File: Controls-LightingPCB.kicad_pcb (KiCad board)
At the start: 2 copper layers, 63.5 x 114.3 mm, 65 parts, among them J1 MinionConn, J2 Backup, SW1 HAZARD, SW2 CRUISE_SET, SW3 CRUISE, SW4 F/R_SW, SW5 HEADLIGHT_SW, SW6 BACKUP_SW, SW7 TURN_SIGNAL_SW, SW8 REGEN_SW, U1 LTC6820, U2 HX1188FNL, U3 MCP23S17_SO, U4 RI3-1205S, U5 NCP1117-3.3_SOT223

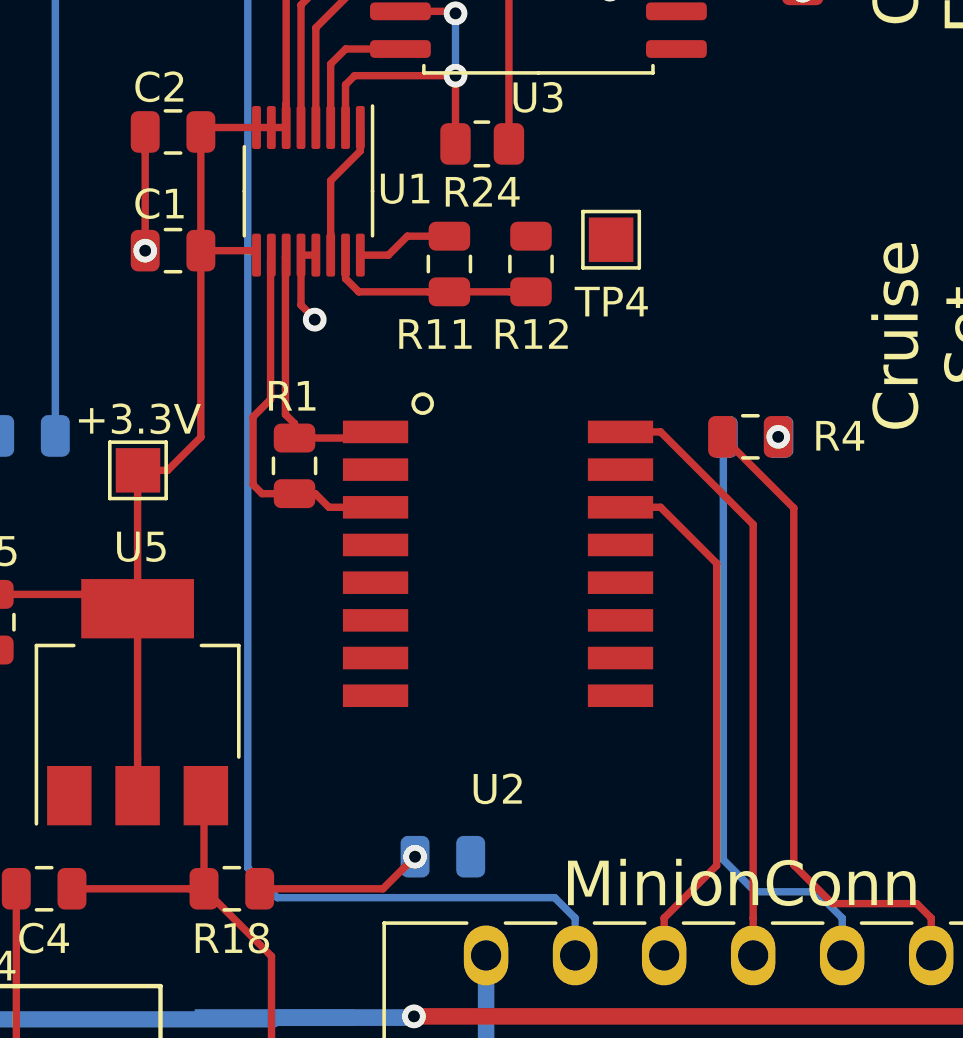
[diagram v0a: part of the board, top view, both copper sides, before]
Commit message: Remove some ground plane underneath isoSPI signals
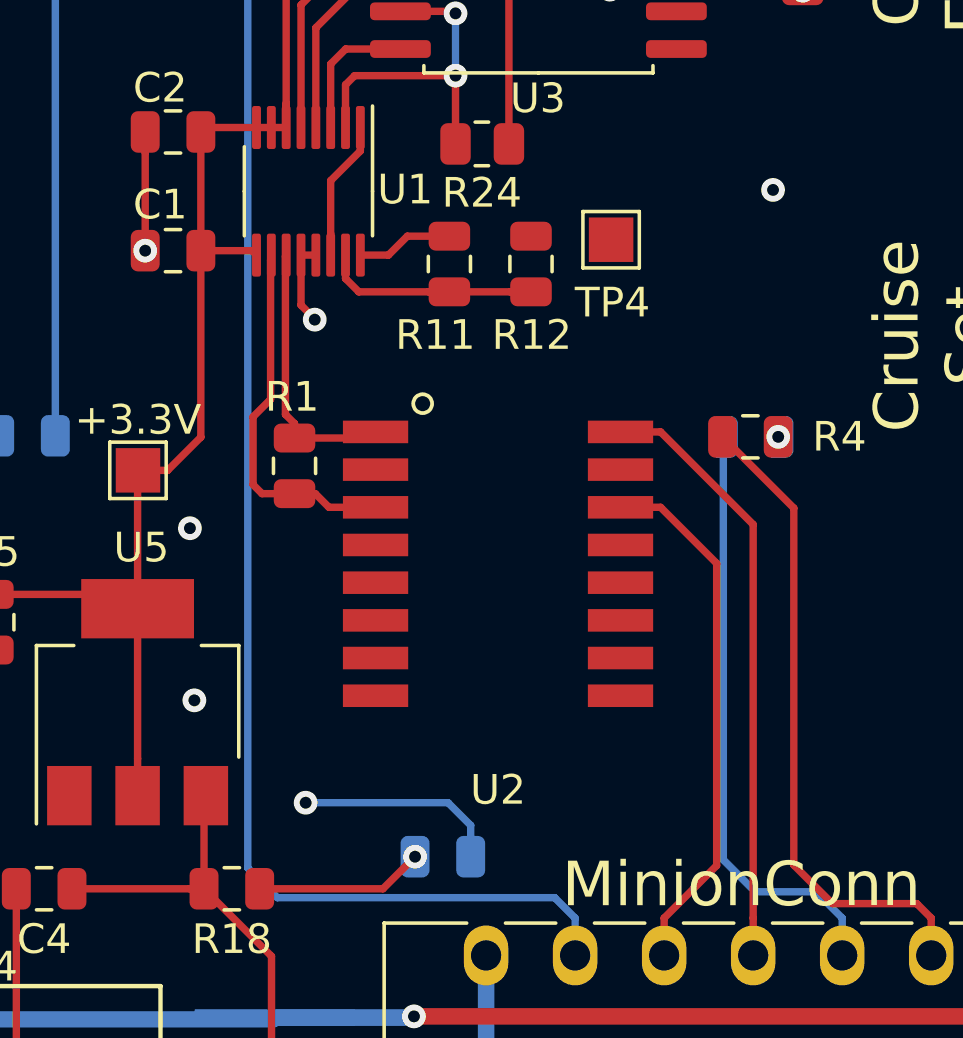
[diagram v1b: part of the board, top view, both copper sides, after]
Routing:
- net GND: track 41.0 -> 48.0 mm, vias 5 -> 9

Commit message: Updates gerbers and version number
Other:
- board text added: "UTSVT - Controls Minion Board v1.1 Fall 2020"
- board text removed: "UTSVT - Controls Minion Board v1.0 Fall 2020"
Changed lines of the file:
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@@
-(kicad_pcb (version 20171130) (host pcbnew 5.1.9+dfsg1-1)
+(kicad_pcb (version 20171130) (host pcbnew "(5.1.5)-3")
   (general
     (thickness 1.6)
@@
     (effects (font (size 1 1) (thickness 0.15)))
   )
-  (gr_text "UTSVT - Controls\nMinion Board v1.0\nFall 2020" (at 165.5 54.1 180) (layer F.SilkS)
+  (gr_text "UTSVT - Controls\nMinion Board v1.1\nFall 2020" (at 165.5 54.1 180) (layer F.SilkS)
     (effects (font (size 1.5 1.5) (thickness 0.3)))
   )

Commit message: Adds the gerbers
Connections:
- U1 pad 13: GND -> +3V3
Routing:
- net +3V3: track 273.4 -> 277.9 mm
- net GND: track 48.0 -> 47.5 mm
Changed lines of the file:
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@@
     (thickness 1.6)
     (drawings 40)
-    (tracks 437)
+    (tracks 441)
     (zones 0)
     (modules 65)
@@
       (net 11 GND))
     (pad 13 smd roundrect (at 2.15 -0.25 270) (size 1.45 0.3) (layers F.Cu F.Paste F.Mask) (roundrect_rratio 0.25)
-      (net 11 GND))
+      (net 10 +3V3))
     (pad 14 smd roundrect (at 2.15 -0.75 270) (size 1.45 0.3) (layers F.Cu F.Paste F.Mask) (roundrect_rratio 0.25)
       (net 11 GND))
@@
   (segment (start 159.61338 118.19662) (end 161.51676 120.1) (width 0.25) (layer F.Cu) (net 10))
   (segment (start 157.16846 115.7517) (end 159.61338 118.19662) (width 0.25) (layer F.Cu) (net 10))
+  (segment (start 153.29346 129.0467) (end 153.29346 127.89346) (width 0.25) (layer F.Cu) (net 10))
+  (segment (start 153.29346 127.89346) (end 153 127.6) (width 0.25) (layer F.Cu) (net 10))
+  (segment (start 153 127.6) (end 151.6 127.6) (width 0.25) (layer F.Cu) (net 10))
+  (segment (start 151.29346 127.90654) (end 151.29346 129.0467) (width 0.25) (layer F.Cu) (net 10))
+  (segment (start 151.6 127.6) (end 151.29346 127.90654) (width 0.25) (layer F.Cu) (net 10))
   (segment (start 153.79346 128.3217) (end 153.79346 129.0467) (width 0.25) (layer F.Cu) (net 11))
   (segment (start 153.79346 126.537402) (end 153.79346 128.3217) (width 0.25) (layer F.Cu) (net 11))
   (segment (start 154.79346 125.537402) (end 153.79346 126.537402) (width 0.25) (layer F.Cu) (net 11))
   (segment (start 154.79346 124.7467) (end 154.79346 125.537402) (width 0.25) (layer F.Cu) (net 11))
-  (segment (start 153.29346 129.0467) (end 152.79346 129.0467) (width 0.25) (layer F.Cu) (net 11))
   (segment (start 152.79346 130.73154) (end 153.256 131.19408) (width 0.25) (layer F.Cu) (net 11))
   (segment (start 147.54346 124.8967) (end 147.54346 125.5967) (width 0.25) (layer F.Cu) (net 11))

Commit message: Footprint edit
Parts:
- U3: value MCP23S17_SO -> MCP23S17_SS; footprint Package_SO:SOIC-28W_7.5x17.9mm_P1.27mm -> Package_SO:SSOP-28_5.3x10.2mm_P0.65mm
- moved U3 4.12 mm to (161.2, 109.8)
- moved D5 0.08 mm to (168.0, 111.0)
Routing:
- net Net-(D5-Pad2): track 31.1 -> 42.5 mm
- net /REV_SW: track 81.0 -> 70.9 mm, vias 3 -> 5
- net /MOSI: track 11.6 -> 21.4 mm
- net /MISO: track 4.70 -> 13.3 mm
- net /SCK: track 6.97 -> 15.1 mm
- net /CS: track 8.44 -> 16.2 mm
- net /HZD_SW: track 80.6 -> 72.9 mm
- net /FOR_SW: track 67.6 -> 60.7 mm
- net +3V3: track 277.9 -> 284.6 mm
- net GND: track 47.5 -> 42.6 mm, vias 9 -> 6
- net Net-(R23-Pad2): track 4.27 -> 8.89 mm
- net /CRUZ_ST: track 37.2 -> 41.3 mm
- net /LEFT_SW: track 51.9 -> 47.9 mm
- net Net-(D3-Pad2): track 0.08 -> 3.55 mm
- net Net-(D7-Pad2): track 0.03 -> 3.37 mm
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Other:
- board text added: "hi~~ :) -nathan"

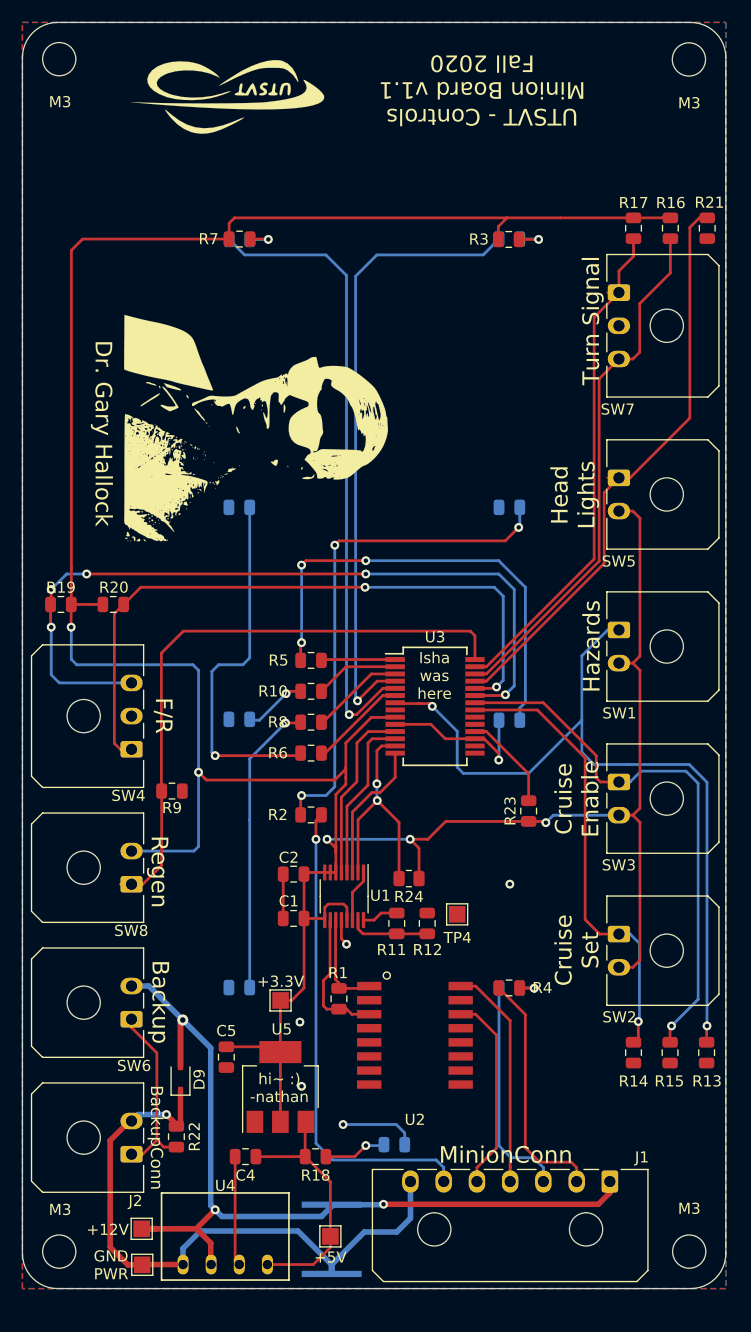
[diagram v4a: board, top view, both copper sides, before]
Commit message: isoSPI -> SPI change
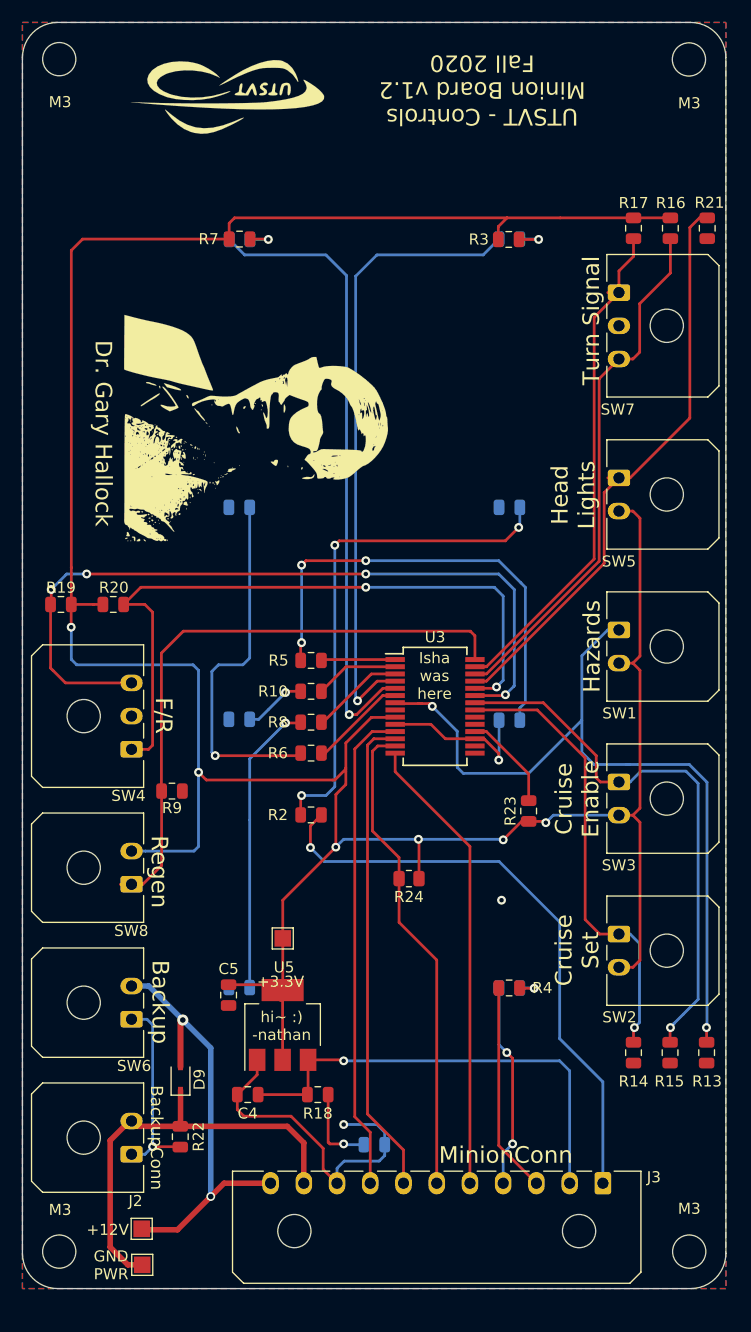
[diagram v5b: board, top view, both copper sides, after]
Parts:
- removed C1, C2: 0.1u, Capacitor_SMD:C_0805_2012Metric
- removed C3: 10u, UTSVT_Passive:C_2220_5750Metric
- removed J1: MinionConn, Connector_Molex:Molex_Micro-Fit_3.0_43650-0700_1x07_P3.00mm_Horizontal
- removed R1: 120, Resistor_SMD:R_0805_2012Metric
- removed R11: 806, Resistor_SMD:R_0805_2012Metric
- removed R12: 1.2k, Resistor_SMD:R_0805_2012Metric
- removed TP3: +5V_TP, TestPoint:TestPoint_Pad_1.5x1.5mm
- removed TP4: GND_TP, TestPoint:TestPoint_Pad_1.5x1.5mm
- removed U1: LTC6820, Package_SO:MSOP-16_3x4mm_P0.5mm
- removed U2: HX1188FNL, UTSVT_Passive:HXXXX
- removed U4: RI3-1205S, UTSVT_ICs:RI3_DC_Converter
- added J3: Conn_01x11, Connector_Molex:Molex_Micro-Fit_3.0_43650-1100_1x11_P3.00mm_Horizontal, F.Cu at (176.4, 152.8)
- moved C5 5.60 mm to (142.6, 135.8)
- moved TP5 5.60 mm to (147.5, 130.7)
- moved C4 5.60 mm to (144.3, 144.8)
- moved R18 5.60 mm to (150.7, 144.8)
- moved U5 5.60 mm to (147.5, 138.5)
- moved D1 1.80 mm to (155.8, 149.3)
- moved R22 0.35 mm to (138.2, 148.6)
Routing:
- net +12V: track 78.2 -> 40.6 mm, vias 3 -> 2
- net /MISO: track 13.3 -> 42.1 mm
- net /SCK: track 15.1 -> 43.6 mm
- net /CS: track 16.2 -> 44.1 mm
- net /MOSI: track 21.4 -> 43.6 mm, vias 2 -> 0
- net Net-(J1-Pad4): track 20.3 -> 0.00 mm
- net GNDPWR: track 58.4 -> 39.5 mm, vias 1 -> 0
- net +5V: track 23.1 -> 41.8 mm, vias 0 -> 1
- net Net-(J1-Pad5): track 18.0 -> 0.00 mm
- net +3V3: track 284.6 -> 267.7 mm, vias 5 -> 6
- net /IM: track 12.3 -> 0.00 mm
- net /BPS_PWR: track 43.6 -> 54.4 mm
- net /IP: track 8.98 -> 0.00 mm
- net Net-(R11-Pad1): track 7.23 -> 0.00 mm
- net Net-(R11-Pad2): track 3.26 -> 0.00 mm
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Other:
- board text added: "UTSVT - Controls Minion Board v1.2 Fall 2020"
- board text removed: "+5V"
- board text removed: "UTSVT - Controls Minion Board v1.1 Fall 2020"

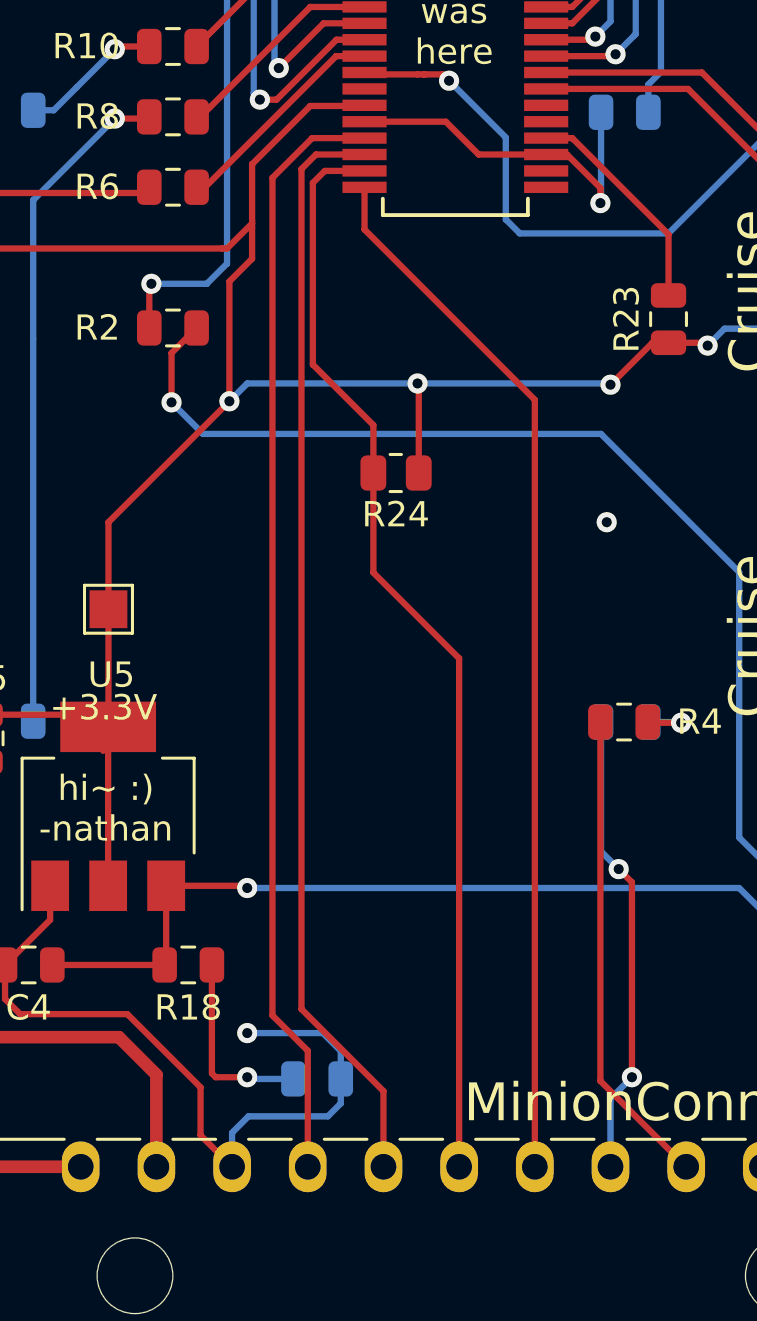
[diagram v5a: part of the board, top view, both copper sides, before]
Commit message: Deleted backup camera
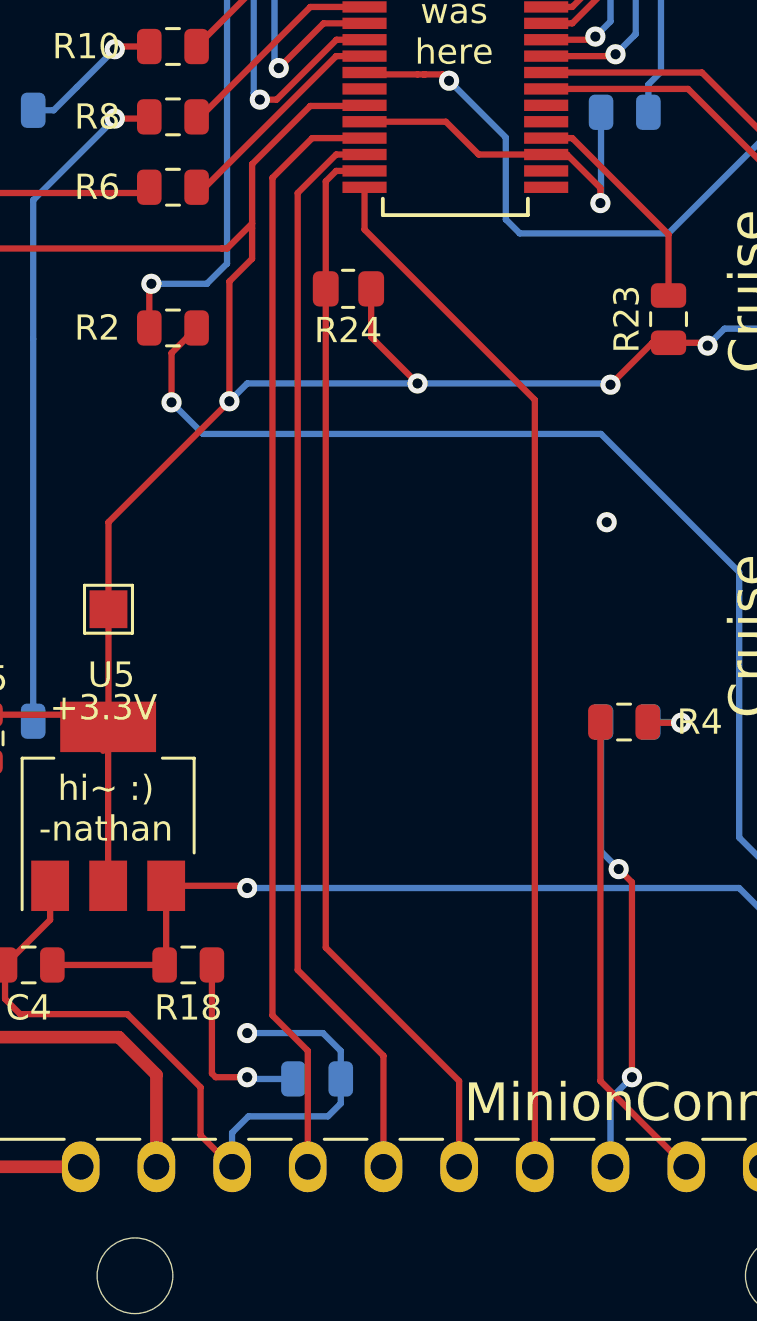
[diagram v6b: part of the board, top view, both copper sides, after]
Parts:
- moved R24 7.54 mm to (157.0, 118.0)
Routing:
- net +3V3: track 267.7 -> 268.7 mm
- net /MOSI: track 43.6 -> 43.0 mm

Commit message: makes changes to traces(11/20/21)
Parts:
- removed D9: TVS, Diode_SMD:D_SOD-323
- removed J2: Backup, Connector_Molex:Molex_Micro-Fit_3.0_43650-0200_1x02_P3.00mm_Horizontal
- removed R22: 10k, Resistor_SMD:R_0805_2012Metric
- removed R24: R, Resistor_SMD:R_0805_2012Metric
- removed SW6: BACKUP_SW, Connector_Molex:Molex_Micro-Fit_3.0_43650-0200_1x02_P3.00mm_Horizontal
- removed TP1: +12V_TP, TestPoint:TestPoint_Pad_1.5x1.5mm
- removed TP2: GNDPWR_TP, TestPoint:TestPoint_Pad_1.5x1.5mm
- added TP3: +5V_TP, TestPoint:TestPoint_Pad_1.5x1.5mm, F.Cu at (176.5, 145.6)
- added TP4: GND_TP, TestPoint:TestPoint_Pad_1.5x1.5mm, F.Cu at (164.7, 148.2)
- D1: moved to F.Cu
- J3: value Conn_01x11 -> MinionConn; footprint Connector_Molex:Molex_Micro-Fit_3.0_43650-1100_1x11_P3.00mm_Horizontal -> Connector_Molex:Molex_Micro-Fit_3.0_43650-0900_1x09_P3.00mm_Horizontal
- moved C5 31.3 mm to (173.6, 140.6)
- moved TP5 31.0 mm to (177.0, 140.3)
- moved C4 29.2 mm to (173.6, 144.3), turned to 90 degrees
- moved R18 23.2 mm to (173.6, 148.7), turned to 270 degrees
- moved D1 20.6 mm to (176.4, 148.6), turned to 270 degrees
- moved U5 20.6 mm to (167.7, 142.3)
- moved J3 6.76 mm to (169.6, 153.0)
- turned D4 to 180 degrees
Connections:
- J3 pad 1: /BPS_PWR -> +5V
- J3 pad 2: +5V -> GND
- J3 pad 3: /BPS_FAULT+ -> /MOSI
- J3 pad 4: /BPS_FAULT- -> /MISO
- J3 pad 5: /MISO -> /SCK
- J3 pad 6: /MOSI -> /CS
- J3 pad 7: /SCK -> /BPS_PWR
- J3 pad 8: /CS -> /BPS_FAULT+
- J3 pad 9: GND -> /BPS_FAULT-
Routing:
- net +12V: track 40.6 -> 0.00 mm, vias 2 -> 0
- net GNDPWR: track 39.5 -> 0.00 mm
- net +5V: track 41.8 -> 16.4 mm, vias 1 -> 0
- net GND: track 45.5 -> 22.4 mm, vias 3 -> 1
- net /BPS_PWR: track 54.4 -> 34.3 mm, vias 1 -> 0
- net /ControlSwitches/Backup: track 17.7 -> 0.00 mm, vias 1 -> 0
- net /BPS_FAULT-: track 19.0 -> 31.5 mm, vias 2 -> 0
- net /BPS_FAULT+: track 19.0 -> 26.3 mm, vias 0 -> 1
- net Net-(D1-Pad2): track 7.62 -> 2.94 mm, vias 1 -> 0
- net Net-(D4-Pad2): track 2.95 -> 7.23 mm
- net +3V3: track 268.7 -> 266.4 mm
- net /MISO: track 42.1 -> 40.7 mm
- net /CS: track 44.1 -> 44.7 mm
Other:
- board text removed: "+12V"
- board text removed: "+3.3V"
- board text removed: "Backup"
- board text removed: "BackupConn"
- board text removed: "GND PWR"

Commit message: Reviews layout
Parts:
- moved TP4 15.8 mm to (180.5, 147.8)
- moved TP5 0.54 mm to (176.5, 140.1)
- moved D1 0.19 mm to (176.5, 148.7)
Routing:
- net /BPS_FAULT-: track 31.5 -> 41.1 mm
- net /BPS_FAULT+: track 26.3 -> 33.9 mm
- net /CS: track 44.7 -> 43.7 mm
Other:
- board text added: "+3.3 V"
- board text added: "+5V"
- board text added: "Aaron was here"
- board text added: "BPS_FAULT+"
- board text added: "BPS_FAULT-"
- board text added: "BPS_PWR"
- board text added: "CLK"
- board text added: "CS"
- board text added: "GND"
- board text added: "Lauren was here"
- board text added: "MISO"
- board text added: "MOSI"
- board text added: "Max was here"
- board text added: "Minion Conn"
- board text added: "Renee was here"
- board text added: "UTSVT - Controls Minion Board v1.4 Fall 2021"
- board text removed: "MinionConn"
- board text removed: "UTSVT - Controls Minion Board v1.2 Fall 2020"
